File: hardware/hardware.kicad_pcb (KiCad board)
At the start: 2 copper layers, 126.5 x 76.2 mm, 6 parts, among them U2 Teensy4.1_DEV-16771, U3 OKI-78SR-3.3_1.5-W36H-C, U4 LT1910, U5 LT1910, U6 LT1910

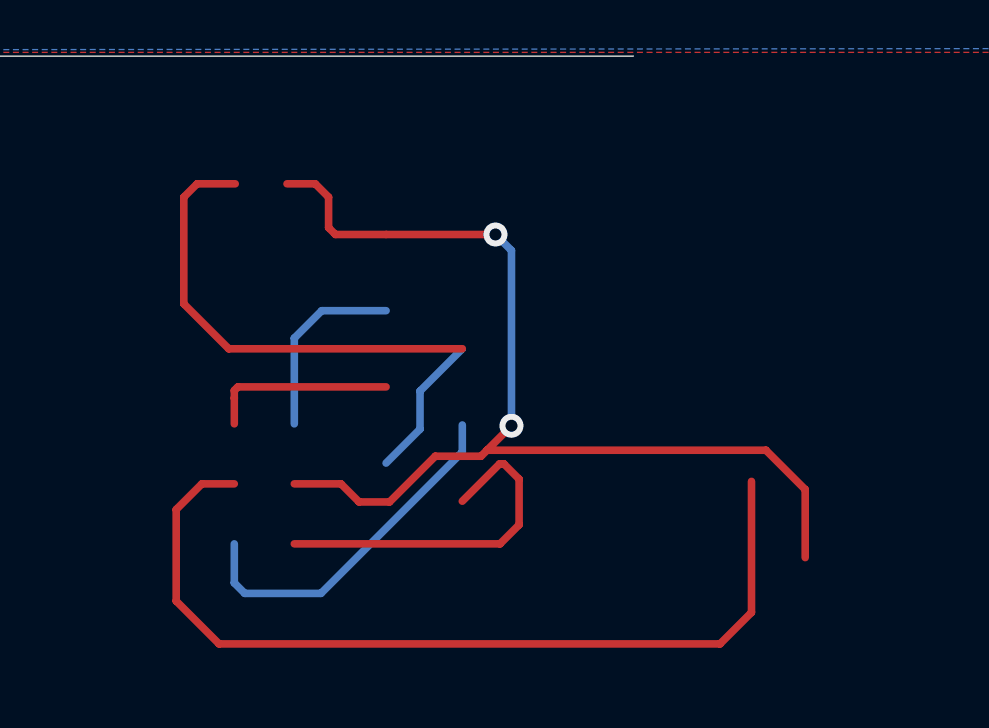
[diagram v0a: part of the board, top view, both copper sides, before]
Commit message: Un-garbaged RJ45 layout
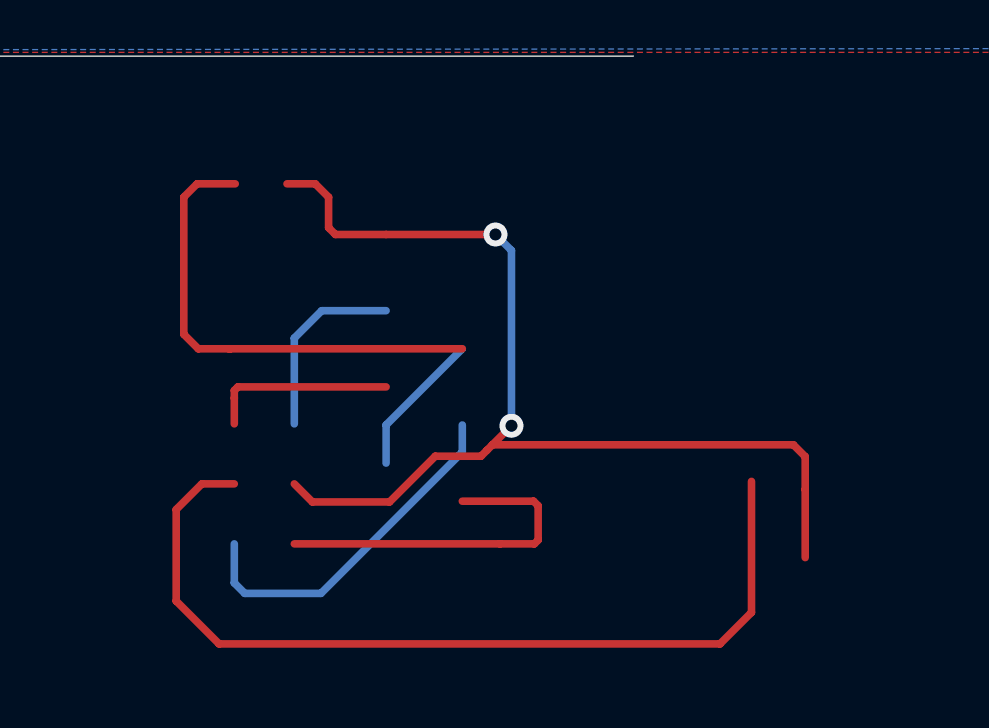
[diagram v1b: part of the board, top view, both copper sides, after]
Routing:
- net Net-(C1-Pad1): track 20.2 -> 20.9 mm
- net Net-(C1-Pad2): track 36.8 -> 37.3 mm
